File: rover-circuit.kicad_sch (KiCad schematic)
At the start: 37 parts, among them J1 Battery, J2 USB_C_Receptacle_USB2.0_14P, J3 Recharge Connector, J4 Display Connector, Q1 AO3401A, SW1 SW_EN, SW2 SW_IO0, SW3 SW_SPDT, U1 LM3671MFX-1.25_NOPB, U2 ESP32-S3-WROOM-1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

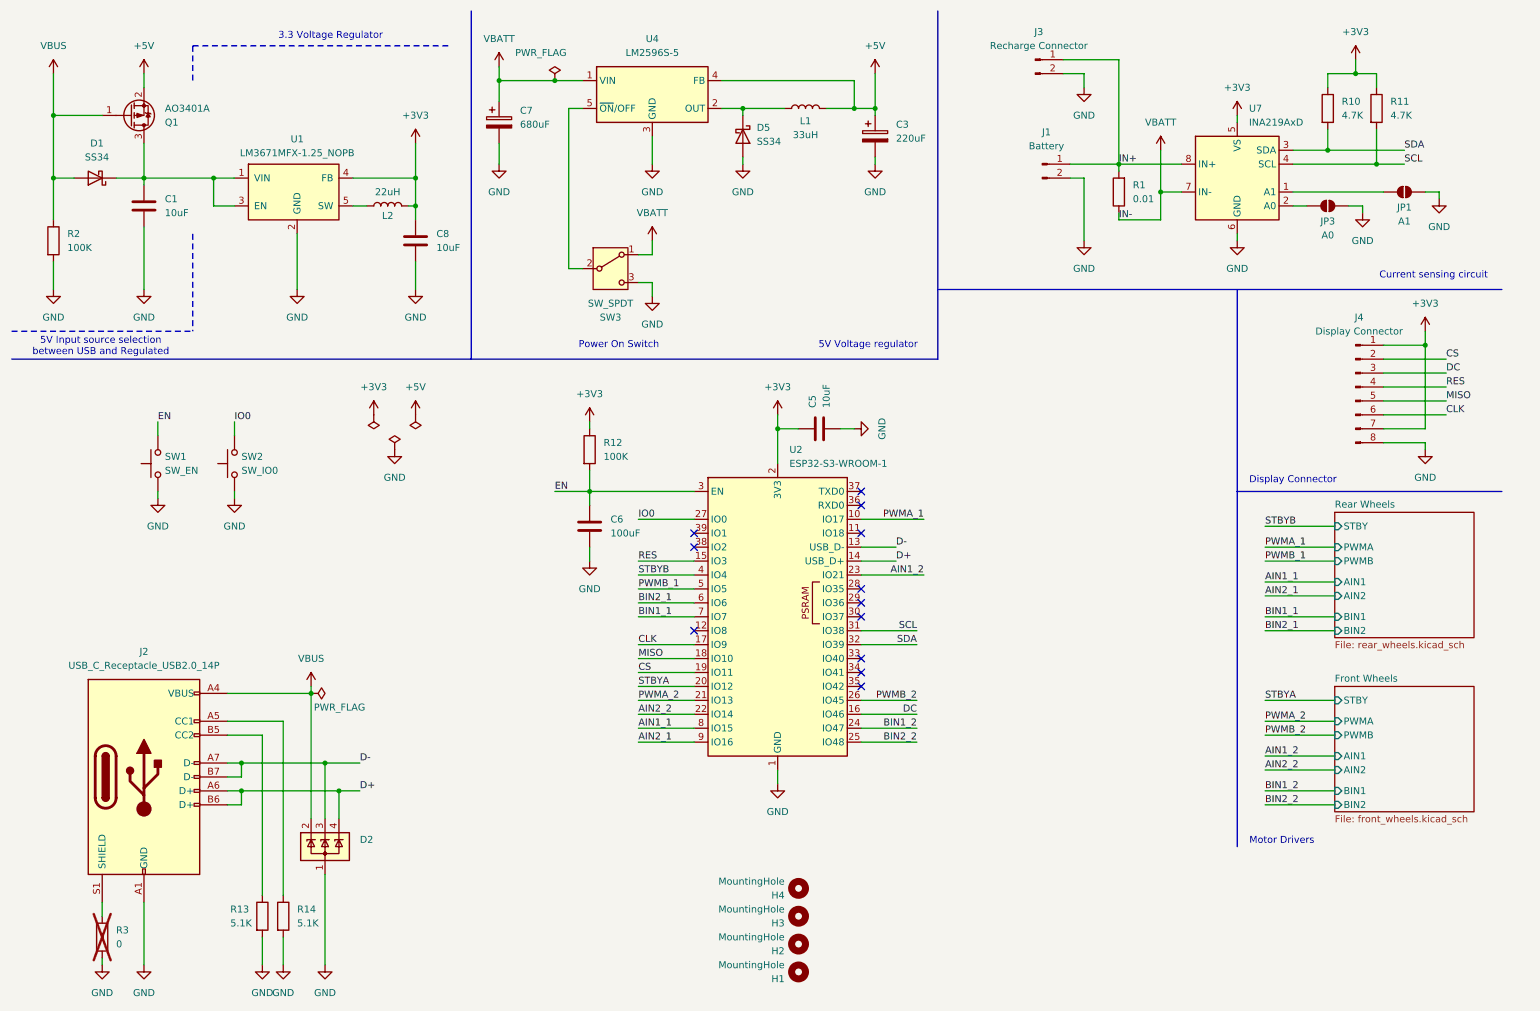
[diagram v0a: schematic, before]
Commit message: finalize components placement
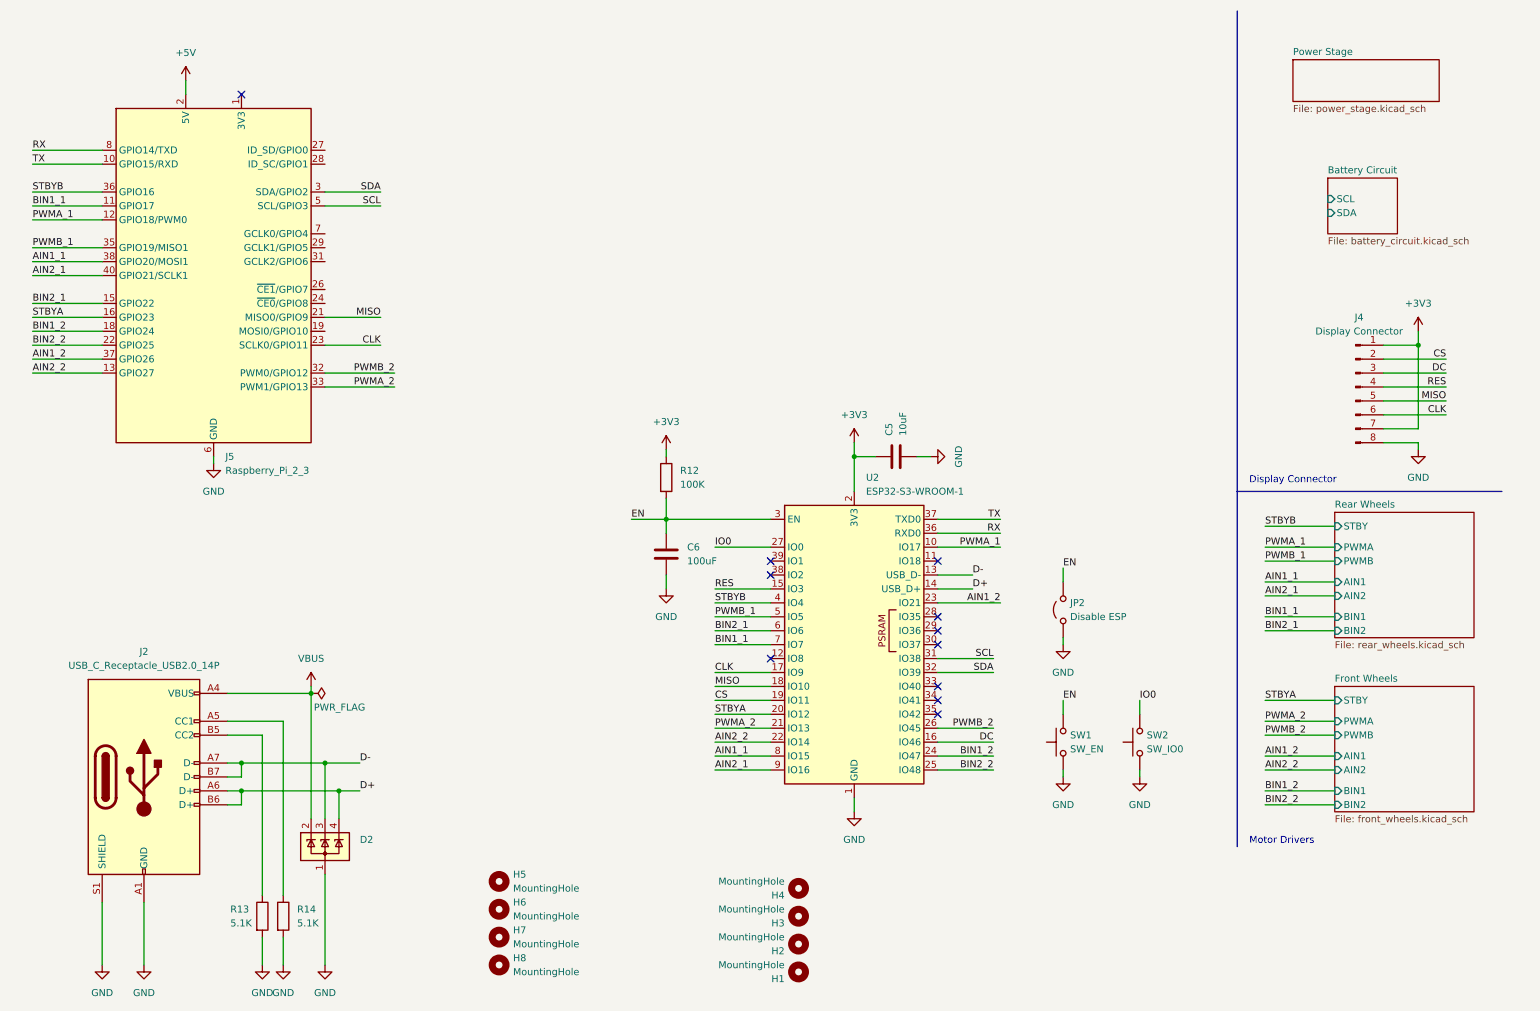
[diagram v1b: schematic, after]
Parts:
- removed C1, C8: 10uF, Capacitor_SMD:C_0805_2012Metric, symbol Device:C
- removed C3: 220uF, Capacitor_SMD:CP_Elec_6.3x7.7, symbol Device:C_Polarized
- removed C7: 680uF, Capacitor_SMD:CP_Elec_10x10, symbol Device:C_Polarized
- removed D1, D5: SS34, Diode_SMD:D_SMA, symbol Diode:SS34
- removed J1: Battery, Connector_JST:JST_EH_S2B-EH_1x02_P2.50mm_Horizontal, symbol Connector:Conn_01x02_Pin
- removed J3: Recharge Connector, Connector_JST:JST_EH_B2B-EH-A_1x02_P2.50mm_Vertical, symbol Connector:Conn_01x02_Pin
- removed JP1: A1, Jumper:SolderJumper-2_P1.3mm_Open_RoundedPad1.0x1.5mm, symbol Jumper:SolderJumper_2_Open
- removed JP3: A0, Jumper:SolderJumper-2_P1.3mm_Open_RoundedPad1.0x1.5mm, symbol Jumper:SolderJumper_2_Open
- removed L1: 33uH, Inductor_SMD:L_10.4x10.4_H4.8, symbol Device:L
- removed L2: 22uH, Inductor_SMD:L_Taiyo-Yuden_MD-5050, symbol Device:L
- removed Q1: AO3401A, Package_TO_SOT_SMD:SOT-23, symbol Transistor_FET:AO3401A
- removed R1: 0.01, Resistor_SMD:R_2512_6332Metric, symbol Device:R
- removed R10, R11: 4.7K, Resistor_SMD:R_0805_2012Metric, symbol Device:R
- removed R2: 100K, Resistor_SMD:R_0805_2012Metric, symbol Device:R
- removed R3: 0, Resistor_SMD:R_0805_2012Metric, symbol Device:R
- removed SW3: SW_SPDT, Button_Switch_THT:SW_Slide_SPDT_Angled_CK_OS102011MA1Q, symbol Switch:SW_SPDT
- removed U1: LM3671MFX-1.25_NOPB, Package_TO_SOT_SMD:SOT-23-5, symbol LM3671MFX-1.25_NOPB:LM3671MFX-1.25_NOPB
- removed U4: LM2596S-5, Package_TO_SOT_SMD:TO-263-5_TabPin3, symbol Regulator_Switching:LM2596S-5
- removed U7: INA219AxD, Package_SO:SOIC-8_3.9x4.9mm_P1.27mm, symbol Sensor_Energy:INA219AxD
- added H5, H6, H7, H8: MountingHole, MountingHole:MountingHole_2.5mm, symbol Mechanical:MountingHole
- added J5: Raspberry_Pi_2_3, Connector_PinSocket_2.54mm:PinSocket_2x20_P2.54mm_Vertical_SMD, symbol Connector:Raspberry_Pi_2_3
- added JP2: Disable ESP, symbol Jumper:Jumper_2_Open
- H1, H2, H3, H4: footprint MountingHole:MountingHole_3.2mm_M3 -> MountingHole:MountingHole_3.2mm_M3_Pad
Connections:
- net +5V: now also J5.2 (5V), J5.4 (5V)
- net AIN1_1: now also J5.38 (GPIO20/MOSI1)
- net AIN1_2: now also J5.37 (GPIO26)
- net AIN2_1: now also J5.40 (GPIO21/SCLK1)
- net AIN2_2: now also J5.13 (GPIO27)
- net BIN1_1: now also J5.11 (GPIO17)
- net BIN1_2: now also J5.18 (GPIO24)
- net BIN2_1: now also J5.15 (GPIO22)
- net BIN2_2: now also J5.22 (GPIO25)
- net CLK: now also J5.23 (SCLK0/GPIO11)
- net EN: now also JP2.2 (B)
- net GND: now also J2.S1 (SHIELD), J5.14 (GND), J5.20 (GND), J5.25 (GND), J5.30 (GND), J5.34 (GND), J5.39 (GND), J5.6 (GND), J5.9 (GND), JP2.1 (A)
- net MISO: now also J5.21 (MISO0/GPIO9)
- net PWMA_1: now also J5.12 (GPIO18/PWM0)
- net PWMA_2: now also J5.33 (PWM1/GPIO13)
- net PWMB_1: now also J5.35 (GPIO19/MISO1)
- net PWMB_2: now also J5.32 (PWM0/GPIO12)
- net SCL: now also J5.5 (SCL/GPIO3)
- net SDA: now also J5.3 (SDA/GPIO2)
- net STBYA: now also J5.16 (GPIO23)
- net STBYB: now also J5.36 (GPIO16)
- net RX: now reaches U2.36 (RXD0)
- net RX: now also J5.8 (GPIO14/TXD)
- net TX: now reaches U2.37 (TXD0)
- net TX: now also J5.10 (GPIO15/RXD)
- new net: J5.1 (3V3), J5.17 (3V3)
- no-connect marks 12 -> 11
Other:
- added sheet Battery Circuit (battery_circuit.kicad_sch)
- added sheet Power Stage (power_stage.kicad_sch)
- note removed: "3.3 Voltage Regulator"
- note removed: "5V Input source selection between USB and Regulated"
- note removed: "5V Voltage regulator"
- note removed: "Current sensing circuit"
- note removed: "Power On Switch"
- moved on the sheet: C5, C6, R12, SW1, SW2, U2

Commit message: some updates
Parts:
- added R2, R6: 4.7K, symbol Device:R
- added TP3: SDA, TestPoint:TestPoint_Pad_D1.0mm, symbol Connector:TestPoint
- added TP4: SCL, TestPoint:TestPoint_Pad_D1.0mm, symbol Connector:TestPoint
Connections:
- net +3V3: now also R2.1, R6.1
- net SCL: now also R2.2, TP4.1
- net SDA: now also R6.2, TP3.1
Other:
- added sheet Motion Tracking (motion_tracking.kicad_sch)
- moved on the sheet: C5, C6, R12, U2

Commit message: add uwb module
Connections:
- net CLK: now also U2.16 (IO46); no longer U2.17 (IO9)
- net CS: no longer U2.19 (IO11)
- net DC: no longer U2.16 (IO46)
- net MISO: now also U2.17 (IO9); no longer U2.18 (IO10)
- net PWMA_2: no longer U2.21 (IO13)
- net RES: no longer U2.15 (IO3)
- net SCL: now also R6.2, U2.35 (IO42); no longer R2.2, U2.31 (IO38)
- net SDA: now also R2.2, U2.34 (IO41); no longer R6.2, U2.32 (IO39)
- net STBYA: no longer U2.20 (IO12)
- net MOSI: now reaches J5.19 (MOSI0/GPIO10)
- net MOSI: now also U2.18 (IO10)
- net UWB_~{CS}: now reaches J5.24 (~{CE0}/GPIO8)
- net UWB_~{CS}: now also U2.19 (IO11)
- new net UWB_IRQ: U2.15 (IO3)
- new net UWB_WU: U2.20 (IO12)
- new net UWB_~{RST}: U2.21 (IO13)
- no-connect marks 11 -> 9
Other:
- added sheet UWB Module (uwb_module.kicad_sch)
- moved on the sheet: TP3, TP4

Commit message: minors
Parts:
- JP2: footprint (none) -> TestPoint:TestPoint_Bridge_Pitch2.54mm_Drill0.7mm
- R2, R6: footprint (none) -> Resistor_SMD:R_0402_1005Metric
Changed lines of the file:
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@@
 			)
 		)
-		(property "Footprint" ""
+		(property "Footprint" "Resistor_SMD:R_0402_1005Metric"
 			(at 174.752 121.92 90)
 			(effects
@@
 			)
 		)
-		(property "Footprint" ""
+		(property "Footprint" "TestPoint:TestPoint_Bridge_Pitch2.54mm_Drill0.7mm"
 			(at 204.47 121.92 0)
 			(effects
@@
 			)
 		)
-		(property "Footprint" ""
+		(property "Footprint" "Resistor_SMD:R_0402_1005Metric"
 			(at 183.642 121.92 90)
 			(effects

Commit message: more routing
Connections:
- net AIN1_2: now also U2.33 (IO40); no longer U2.23 (IO21)
- net AIN2_2: now also U2.32 (IO39); no longer J5.13 (GPIO27), U2.22 (IO14)
- net BIN1_1: now also U2.6 (IO6); no longer J5.11 (GPIO17), U2.7 (IO7)
- net BIN1_2: now also U2.35 (IO42); no longer J5.18 (GPIO24), U2.24 (IO47)
- net BIN2_1: now also U2.5 (IO5); no longer J5.15 (GPIO22), U2.6 (IO6)
- net BIN2_2: now also U2.38 (IO2); no longer U2.25 (IO48)
- net CS: now also J5.7 (GCLK0/GPIO4), U2.24 (IO47)
- net DC: now also J5.11 (GPIO17), U2.23 (IO21)
- net PWMA_2: now also U2.31 (IO38)
- net PWMB_1: now also U2.4 (IO4); no longer U2.5 (IO5)
- net PWMB_2: now also U2.39 (IO1); no longer U2.26 (IO45)
- net RES: now also J5.13 (GPIO27), U2.22 (IO14)
- net SCL: now also U2.26 (IO45); no longer U2.35 (IO42)
- net SDA: now also U2.25 (IO48); no longer U2.34 (IO41)
- net STBYA: now also U2.34 (IO41)
- net STBYB: now also U2.7 (IO7); no longer U2.4 (IO4)
- net UWB_IRQ: now also J5.26 (~{CE1}/GPIO7)
- net UWB_WU: now also J5.18 (GPIO24)
- net UWB_~{RST}: now also J5.15 (GPIO22)
- no-connect marks 9 -> 6
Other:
- moved on the sheet: TP3, TP4

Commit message: more on routing
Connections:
- net AIN1_1: now also J5.22 (GPIO25); no longer J5.38 (GPIO20/MOSI1)
- net AIN1_2: now also J5.36 (GPIO16); no longer J5.37 (GPIO26)
- net AIN2_1: now also J5.16 (GPIO23); no longer J5.40 (GPIO21/SCLK1)
- net AIN2_2: now also J5.31 (GCLK2/GPIO6)
- net BIN1_1: now also J5.28 (ID_SC/GPIO1)
- net BIN1_2: now also J5.40 (GPIO21/SCLK1)
- net BIN2_1: now also J5.29 (GCLK1/GPIO5)
- net BIN2_2: now also J5.37 (GPIO26); no longer J5.22 (GPIO25)
- net PWMB_1: now also J5.32 (PWM0/GPIO12); no longer J5.35 (GPIO19/MISO1)
- net PWMB_2: now also J5.35 (GPIO19/MISO1); no longer J5.32 (PWM0/GPIO12)
- net STBYA: now also J5.38 (GPIO20/MOSI1); no longer J5.16 (GPIO23)
- net STBYB: now also J5.27 (ID_SD/GPIO0); no longer J5.36 (GPIO16)

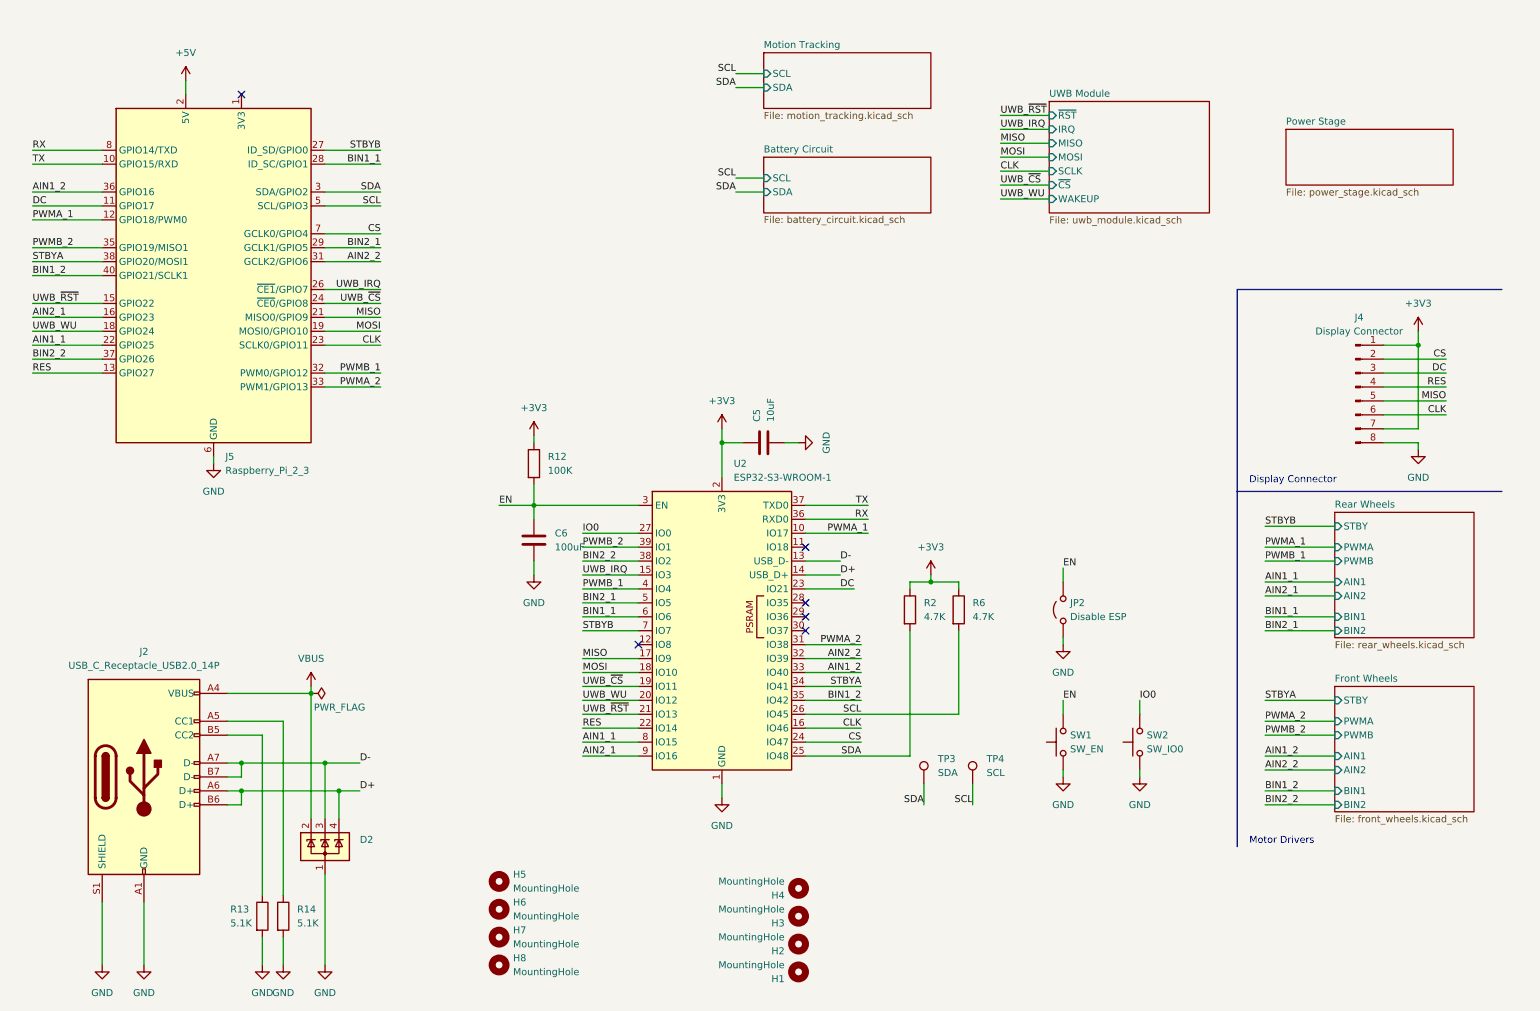
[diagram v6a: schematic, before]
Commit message: finalize routing
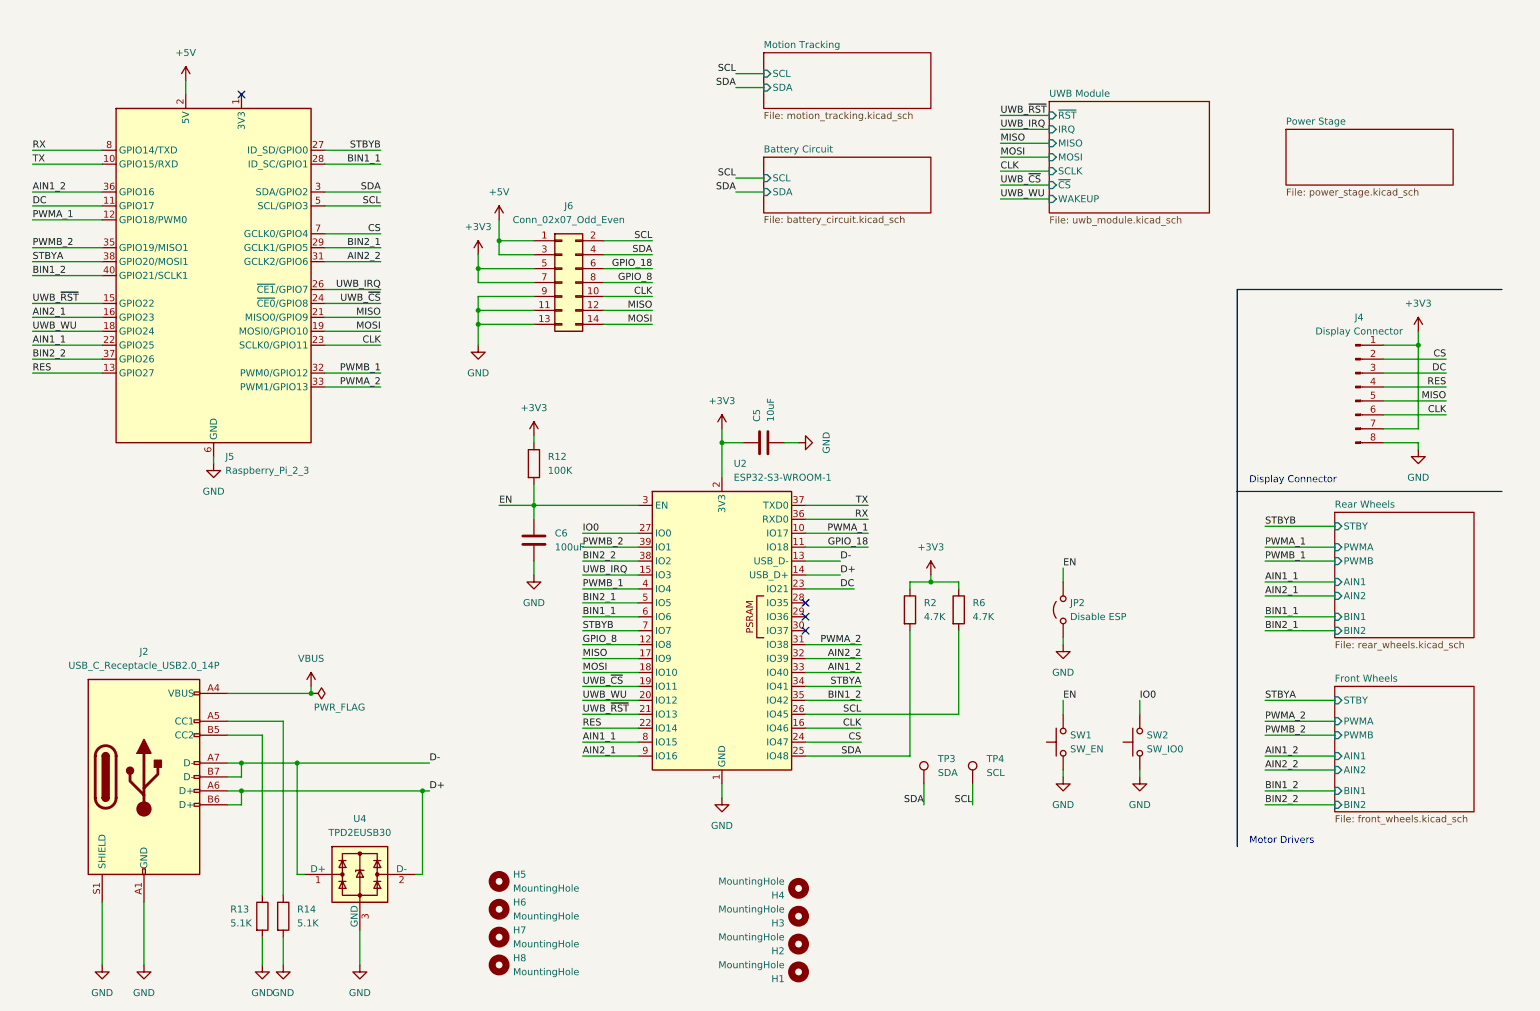
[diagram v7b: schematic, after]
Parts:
- removed D2: SP0503BAHT, Package_TO_SOT_SMD:SOT-143, symbol Power_Protection:SP0503BAHT
- added J6: Conn_02x07_Odd_Even, Connector_PinHeader_2.54mm:PinHeader_2x07_P2.54mm_Vertical, symbol Connector_Generic:Conn_02x07_Odd_Even
- added U4: TPD2EUSB30, Package_TO_SOT_SMD:Texas_DRT-3, symbol Power_Protection:TPD2EUSB30
- JP2: footprint TestPoint:TestPoint_Bridge_Pitch2.54mm_Drill0.7mm -> Connector_PinHeader_2.54mm:PinHeader_1x02_P2.54mm_Vertical
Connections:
- net +3V3: now also J6.5 (Pin_5), J6.7 (Pin_7)
- net +5V: now also J6.1 (Pin_1), J6.3 (Pin_3)
- net CLK: now also J6.10 (Pin_10)
- net D+: now also U4.2 (D-)
- net D-: now also U4.1 (D+)
- net GND: now also J6.11 (Pin_11), J6.13 (Pin_13), J6.9 (Pin_9), U4.3 (GND)
- net MISO: now also J6.12 (Pin_12)
- net MOSI: now also J6.14 (Pin_14)
- net SCL: now also J6.2 (Pin_2)
- net SDA: now also J6.4 (Pin_4)
- net GPIO_18: now reaches U2.11 (IO18)
- net GPIO_18: now also J6.6 (Pin_6)
- net GPIO_8: now reaches U2.12 (IO8)
- net GPIO_8: now also J6.8 (Pin_8)
- no-connect marks 6 -> 4
